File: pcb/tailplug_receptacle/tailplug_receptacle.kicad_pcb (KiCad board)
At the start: 2 copper layers, 25.5 x 25 mm, 6 parts, among them J1 Conn_01x08_MountingPin

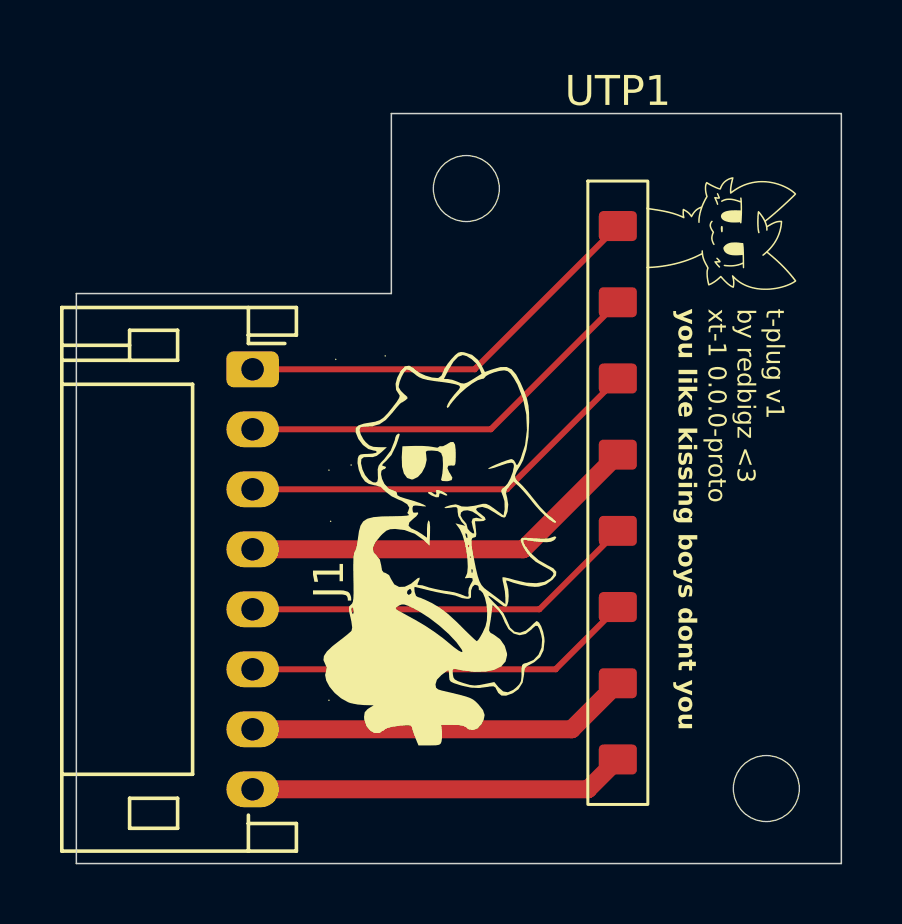
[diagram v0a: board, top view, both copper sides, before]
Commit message: Replace boykissers on PCBs with my pfp (copyright reasons :3)
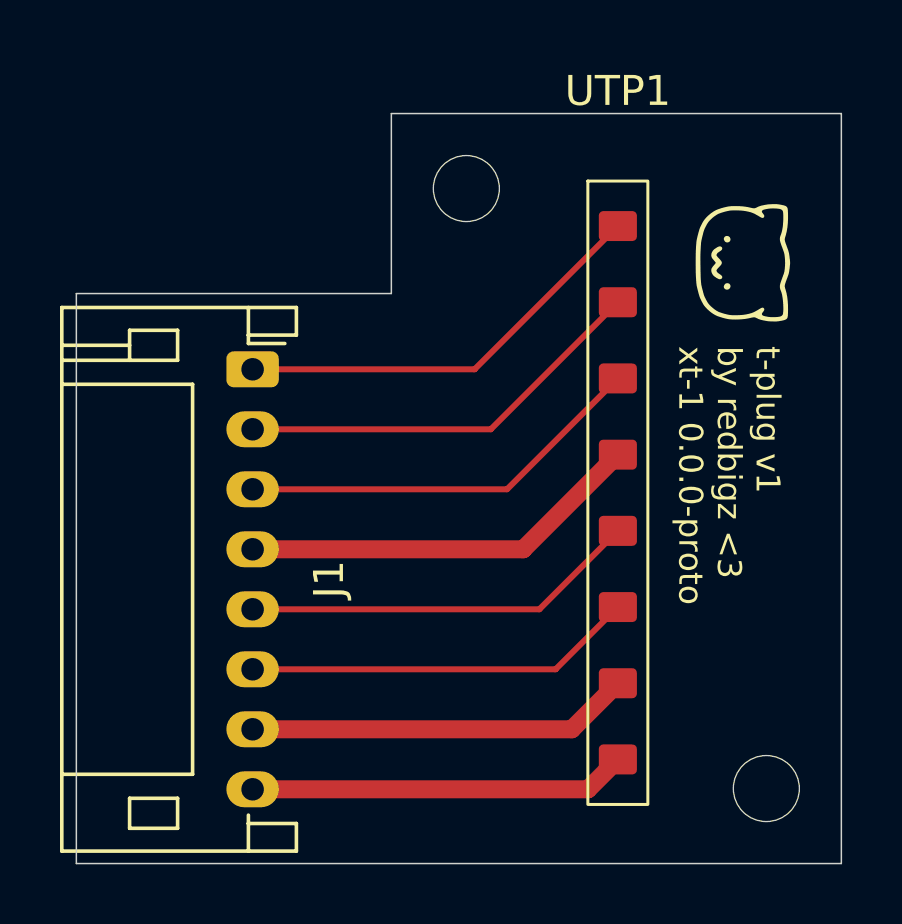
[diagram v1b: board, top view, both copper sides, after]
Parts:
- removed the G*** at (29.0, 30.0)
- removed the G*** at (38.5, 19.5)
- added G***: LOGO, LOGO, F.Cu at (39.2, 20.5)
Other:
- board text removed: "you like kissing boys dont you"
